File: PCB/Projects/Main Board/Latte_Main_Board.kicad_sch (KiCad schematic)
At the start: 115 parts, among them J1 SM02B-SURS-TF_LF__SN_, J2 SM02B-SURS-TF_LF__SN_, J3 Molex 505110-0892, J4 Molex 505110-0592, J5 Molex 505110-0892, J6 Molex 505110-0592, J8 Conn_01x04_Pin, J9 Molex 505110-1792, Q1 MMBT2222A, Q2 MMBT2222A, SW1 SW_Push, SW2 SW_Push, SW3 SW_Push, SW4 SW_Push, SW5 SW_Push, SW6 SW_Push, SW7 SW_Push, SW8 SW_Push, U1 HAL4395, U10 HAL4395, U11 HAL4395, U2 RP2350_80QFN, U3 HAL4395, U4 ST_LSM6, U5 ST_LSM6, U6 HAL4395, U7 HAL4395, U8 HAL4395, U9 HAL4395, Y1 ABM8-272-T3

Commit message: Routing updates
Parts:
- added R25, R28, R29, R31: 100R, Resistor_SMD:R_0201_0603Metric, symbol Device:R
- C39, C40: footprint RP2350_80QFN_minimal:C_0402_1005Metric_small_pads -> Capacitor_SMD:C_0402_1005Metric
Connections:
- net +3V3: now also C17.1, C18.1, C3.1, C4.1, C5.1, C6.1, C7.1, C8.1, U1.1 (VCC), U10.1 (VCC), U11.1 (VCC), U3.1 (VCC), U6.1 (VCC), U7.1 (VCC), U8.1 (VCC), U9.1 (VCC)
- net ABXY_EN: now also R31.2
- net DPAD_EN: now also R25.2
- net LRA_R: now also U2.26 (GPIO25); no longer U2.25 (GPIO24)
- net STICK_L_X_OUT: now also U2.57 (GPIO46_ADC6); no longer U2.56 (GPIO45_ADC5)
- net STICK_L_Y_OUT: now also U2.58 (GPIO47_ADC7); no longer U2.55 (GPIO44_ADC4)
- net STICK_R_X_OUT: now also U2.56 (GPIO45_ADC5); no longer U2.58 (GPIO47_ADC7)
- net STICK_R_Y_OUT: now also U2.55 (GPIO44_ADC4); no longer U2.57 (GPIO46_ADC6)
- net at R21.1: now also U2.37 (GPIO29); no longer U2.36 (GPIO28)
- net at R23.1: now also U2.48 (GPIO39); no longer U2.38 (GPIO30)
- net at U2.12 (GPIO13): now also R25.1
- net at U2.13 (GPIO14): now also R28.1
- net at R2.1: now also U2.27 (GPIO26); no longer U2.26 (GPIO25)
- net at U2.28 (GPIO27): now also R31.1
- net at R24.1: now also U2.36 (GPIO28); no longer U2.37 (GPIO29)
- net TRIGGER_EN renamed TRIGGER_EN_L
- net TRIGGER_EN_L: now also R28.2; no longer J4.2 (Pin_2)
- new net: R29.1, U2.25 (GPIO24)
- new net TRIGGER_EN_R: J4.2 (Pin_2), R29.2
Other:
- note added: "PWM4 B"
- note removed: "PWM4 A"
- moved on the sheet: R2, R21, R23, R24

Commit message: Routing Updates
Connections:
- net LRA_R+: now also J1.2; no longer J1.1
- net LRA_R-: now also J1.1; no longer J1.2
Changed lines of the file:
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@@
 	(global_label "LRA_R-"
 		(shape input)
+		(at 302.26 34.29 0)
+		(fields_autoplaced yes)
+		(effects
+			(font
+				(size 1.27 1.27)
+			)
+			(justify left)
+		)
+		(property "Intersheetrefs" "${INTERSHEET_REFS}"
+			(at 312.4419 34.29 0)
+			(effects
+				(font
+					(size 1.27 1.27)
+				)
+				(justify left)
+				(hide yes)
+			)
+		)
+	)
+	(global_label "ADC_2"
+		(shape input)
+		(at 139.7 -36.83 0)
+		(fields_autoplaced yes)
+		(effects
+			(font
+				(size 1.27 1.27)
+			)
+			(justify left)
+		)
+		(property "Intersheetrefs" "${INTERSHEET_REFS}"
+			(at 148.4909 -36.83 0)
+			(effects
+				(font
+					(size 1.27 1.27)
+				)
+				(justify left)
+				(hide yes)
+			)
+		)
+	)
+	(global_label "I2C1_SCL"
+		(shape input)
+		(at 204.47 130.81 0)
+		(fields_autoplaced yes)
+		(effects
+			(font
+				(size 1.27 1.27)
+			)
+			(justify left)
+		)
+		(property "Intersheetrefs" "${INTERSHEET_REFS}"
+			(at 216.2242 130.81 0)
+			(effects
+				(font
+					(size 1.27 1.27)
+				)
+				(justify left)
+				(hide yes)
+			)
+		)
+	)
+	(global_label "WL_CLK"
+		(shape input)
+		(at 148.59 139.7 0)
+		(fields_autoplaced yes)
+		(effects
+			(font
+				(size 1.27 1.27)
+			)
+			(justify left)
+		)
+		(property "Intersheetrefs" "${INTERSHEET_REFS}"
+			(at 157.9362 139.7 0)
+			(effects
+				(font
+					(size 1.27 1.27)
+				)
+				(justify left)
+				(hide yes)
+			)
+		)
+	)
+	(global_label "SPI1_RX"
+		(shape input)
+		(at 441.96 113.03 180)
+		(fields_autoplaced yes)
+		(effects
+			(font
+				(size 1.27 1.27)
+			)
+			(justify right)
+		)
+		(property "Intersheetrefs" "${INTERSHEET_REFS}"
+			(at 431.2339 113.03 0)
+			(effects
+				(font
+					(size 1.27 1.27)
+				)
+				(justify right)
+				(hide yes)
+			)
+		)
+	)
+	(global_label "STICK_R_RGB_OUT"
+		(shape input)
+		(at 290.83 227.33 180)
+		(fields_autoplaced yes)
+		(effects
+			(font
+				(size 1.27 1.27)
+			)
+			(justify right)
+		)
+		(property "Intersheetrefs" "${INTERSHEET_REFS}"
+			(at 270.9115 227.33 0)
+			(effects
+				(font
+					(size 1.27 1.27)
+				)
+				(justify right)
+				(hide yes)
+			)
+		)
+	)
+	(global_label "N_DATA_3.3"
+		(shape input)
+		(at 204.47 128.27 0)
+		(fields_autoplaced yes)
+		(effects
+			(font
+				(size 1.27 1.27)
+			)
+			(justify left)
+		)
+		(property "Intersheetrefs" "${INTERSHEET_REFS}"
+			(at 217.4985 128.3494 0)
+			(effects
+				(font
+					(size 1.27 1.27)
+				)
+				(justify left)
+				(hide yes)
+			)
+		)
+	)
+	(global_label "SWD"
+		(shape input)
+		(at 73.66 189.23 180)
+		(fields_autoplaced yes)
+		(effects
+			(font
+				(size 1.27 1.27)
+			)
+			(justify right)
+		)
+		(property "Intersheetrefs" "${INTERSHEET_REFS}"
+			(at 66.7439 189.23 0)
+			(effects
+				(font
+					(size 1.27 1.27)
+				)
+				(justify right)
+				(hide yes)
+			)
+		)
+	)
+	(global_label "I2C1_SDA"
+		(shape input)
+		(at 443.23 90.17 270)
+		(fields_autoplaced yes)
+		(effects
+			(font
+				(size 1.27 1.27)
+			)
+			(justify right)
+		)
+		(property "Intersheetrefs" "${INTERSHEET_REFS}"
+			(at 443.23 101.3305 90)
+			(effects
+				(font
+					(size 1.27 1.27)
+				)
+				(justify right)
+				(hide yes)
+			)
+		)
+	)
+	(global_label "ADC_0"
+		(shape input)
+		(at 139.7 -72.39 0)
+		(fields_autoplaced yes)
+		(effects
+			(font
+				(size 1.27 1.27)
+			)
+			(justify left)
+		)
+		(property "Intersheetrefs" "${INTERSHEET_REFS}"
+			(at 148.4909 -72.39 0)
+			(effects
+				(font
+					(size 1.27 1.27)
+				)
+				(justify left)
+				(hide yes)
+			)
+		)
+	)
+	(global_label "LRA_L"
+		(shape input)
+		(at 157.48 152.4 0)
+		(fields_autoplaced yes)
+		(effects
+			(font
+				(size 1.27 1.27)
+			)
+			(justify left)
+		)
+		(property "Intersheetrefs" "${INTERSHEET_REFS}"
+			(at 165.8476 152.4 0)
+			(effects
+				(font
+					(size 1.27 1.27)
+				)
+				(justify left)
+				(hide yes)
+			)
+		)
+	)
+	(global_label "LRA_R+"
+		(shape input)
 		(at 302.26 31.75 0)
 		(fields_autoplaced yes)
@@
 			(effects
 				(font
-					(size 1.27 1.27)
-				)
-				(justify left)
-				(hide yes)
-			)
-		)
-	)
-	(global_label "ADC_2"
-		(shape input)
-		(at 139.7 -36.83 0)
-		(fields_autoplaced yes)
-		(effects
-			(font
-				(size 1.27 1.27)
-			)
-			(justify left)
-		)
-		(property "Intersheetrefs" "${INTERSHEET_REFS}"
-			(at 148.4909 -36.83 0)
-			(effects
-				(font
-					(size 1.27 1.27)
-				)
-				(justify left)
-				(hide yes)
-			)
-		)
-	)
-	(global_label "I2C1_SCL"
-		(shape input)
-		(at 204.47 130.81 0)
-		(fields_autoplaced yes)
-		(effects
-			(font
-				(size 1.27 1.27)
-			)
-			(justify left)
-		)
-		(property "Intersheetrefs" "${INTERSHEET_REFS}"
-			(at 216.2242 130.81 0)
-			(effects
-				(font
-					(size 1.27 1.27)
-				)
-				(justify left)
-				(hide yes)
-			)
-		)
-	)
-	(global_label "WL_CLK"
-		(shape input)
-		(at 148.59 139.7 0)
-		(fields_autoplaced yes)
-		(effects
-			(font
-				(size 1.27 1.27)
-			)
-			(justify left)
-		)
-		(property "Intersheetrefs" "${INTERSHEET_REFS}"
-			(at 157.9362 139.7 0)
-			(effects
-				(font
-					(size 1.27 1.27)
-				)
-				(justify left)
-				(hide yes)
-			)
-		)
-	)
-	(global_label "SPI1_RX"
-		(shape input)
-		(at 441.96 113.03 180)
-		(fields_autoplaced yes)
-		(effects
-			(font
-				(size 1.27 1.27)
-			)
-			(justify right)
-		)
-		(property "Intersheetrefs" "${INTERSHEET_REFS}"
-			(at 431.2339 113.03 0)
-			(effects
-				(font
-					(size 1.27 1.27)
-				)
-				(justify right)
-				(hide yes)
-			)
-		)
-	)
-	(global_label "STICK_R_RGB_OUT"
-		(shape input)
-		(at 290.83 227.33 180)
-		(fields_autoplaced yes)
-		(effects
-			(font
-				(size 1.27 1.27)
-			)
-			(justify right)
-		)
-		(property "Intersheetrefs" "${INTERSHEET_REFS}"
-			(at 270.9115 227.33 0)
-			(effects
-				(font
-					(size 1.27 1.27)
-				)
-				(justify right)
-				(hide yes)
-			)
-		)
-	)
-	(global_label "N_DATA_3.3"
-		(shape input)
-		(at 204.47 128.27 0)
-		(fields_autoplaced yes)
-		(effects
-			(font
-				(size 1.27 1.27)
-			)
-			(justify left)
-		)
-		(property "Intersheetrefs" "${INTERSHEET_REFS}"
-			(at 217.4985 128.3494 0)
-			(effects
-				(font
-					(size 1.27 1.27)
-				)
-				(justify left)
-				(hide yes)
-			)
-		)
-	)
-	(global_label "SWD"
-		(shape input)
-		(at 73.66 189.23 180)
-		(fields_autoplaced yes)
-		(effects
-			(font
-				(size 1.27 1.27)
-			)
-			(justify right)
-		)
-		(property "Intersheetrefs" "${INTERSHEET_REFS}"
-			(at 66.7439 189.23 0)
-			(effects
-				(font
-					(size 1.27 1.27)
-				)
-				(justify right)
-				(hide yes)
-			)
-		)
-	)
-	(global_label "I2C1_SDA"
-		(shape input)
-		(at 443.23 90.17 270)
-		(fields_autoplaced yes)
-		(effects
-			(font
-				(size 1.27 1.27)
-			)
-			(justify right)
-		)
-		(property "Intersheetrefs" "${INTERSHEET_REFS}"
-			(at 443.23 101.3305 90)
-			(effects
-				(font
-					(size 1.27 1.27)
-				)
-				(justify right)
-				(hide yes)
-			)
-		)
-	)
-	(global_label "ADC_0"
-		(shape input)
-		(at 139.7 -72.39 0)
-		(fields_autoplaced yes)
-		(effects
-			(font
-				(size 1.27 1.27)
-			)
-			(justify left)
-		)
-		(property "Intersheetrefs" "${INTERSHEET_REFS}"
-			(at 148.4909 -72.39 0)
-			(effects
-				(font
-					(size 1.27 1.27)
-				)
-				(justify left)
-				(hide yes)
-			)
-		)
-	)
-	(global_label "LRA_L"
-		(shape input)
-		(at 157.48 152.4 0)
-		(fields_autoplaced yes)
-		(effects
-			(font
-				(size 1.27 1.27)
-			)
-			(justify left)
-		)
-		(property "Intersheetrefs" "${INTERSHEET_REFS}"
-			(at 165.8476 152.4 0)
-			(effects
-				(font
-					(size 1.27 1.27)
-				)
-				(justify left)
-				(hide yes)
-			)
-		)
-	)
-	(global_label "LRA_R+"
-		(shape input)
-		(at 302.26 34.29 0)
-		(fields_autoplaced yes)
-		(effects
-			(font
-				(size 1.27 1.27)
-			)
-			(justify left)
-		)
-		(property "Intersheetrefs" "${INTERSHEET_REFS}"
-			(at 312.4419 34.29 0)
-			(effects
-				(font

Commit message: Routing updates
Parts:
- U4, U5: LCSC C784817 -> C126672; MPN LSM6DSRTR -> LSM6DSLTR
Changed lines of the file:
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@@
 			)
 		)
-		(property "LCSC" "C784817"
+		(property "LCSC" "C126672"
 			(at 453.39 156.21 0)
 			(effects
@@
 			)
 		)
-		(property "MPN" "LSM6DSRTR"
+		(property "MPN" "LSM6DSLTR"
 			(at 453.39 156.21 0)
 			(effects
@@
 			)
 		)
-		(property "LCSC" "C784817"
+		(property "LCSC" "C126672"
 			(at 453.39 116.84 0)
 			(effects
@@
 			)
 		)
-		(property "MPN" "LSM6DSRTR"
+		(property "MPN" "LSM6DSLTR"
 			(at 453.39 116.84 0)
 			(effects

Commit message: Routing updates
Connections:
- net GND: now also SW3.1, SW4.1, SW5.1, SW6.1, SW7.1, SW8.1, U2.81 (GND)
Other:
- moved on the sheet: SW5, SW6, SW7, SW8

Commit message: Routing updates
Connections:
- net GND: now also SW2.1; no longer R15.2
- net at R15.1: now also U2.35 (RUN); no longer SW2.1
- net at SW2.2: now also R15.2; no longer U2.35 (RUN)
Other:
- moved on the sheet: C10, C11, C12, C13, C14, C17, C18, C19, C23, C24, C25, C26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

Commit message: Prod 1
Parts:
- C17, C18, C19, C29, C3, C30, C31, C32, C33, C34, C35, C36, C37, C38, C4, C5, C6, C7, C8: LCSC (none) -> C76934; MPN (none) -> GRM033R61A104KE15D; Manufacturer (none) -> muRata
- C23, C39, C40, C41: LCSC (none) -> C541464; MPN (none) -> CC0402JRX7R7BB104; Manufacturer (none) -> YAGEO
- L1: LCSC (none) -> C42411119; MPN (none) -> AOTA-B201610S3R3-101-T; Manufacturer (none) -> Abraco LLC
- R11: LCSC (none) -> C295794; MPN (none) -> RC0201FR-0733RL; Manufacturer (none) -> YAGEO
- R15: LCSC (none) -> C138165; MPN (none) -> RC0201FR-071KL; Manufacturer (none) -> YAGEO
- SW1, SW2, SW3, SW4, SW5, SW6, SW7, SW8: LCSC (none) -> C221725; Manufacturer (none) -> C&K
- U1, U10, U11, U3, U6, U7, U8, U9: LCSC (none) -> C49165022; MPN (none) -> HAL4395SO5; Manufacturer (none) -> Hallwee
- U2: LCSC (none) -> C39843328; MPN (none) -> RP2354B; Manufacturer (none) -> Raspberry Pi

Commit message: 3D Files Initial STLs
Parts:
- C23, C39, C40, C41: LCSC C541464 -> C368809; MPN CC0402JRX7R7BB104 -> CL05A475KP5NRNC; Manufacturer YAGEO -> Samsung Electro-Mechanics
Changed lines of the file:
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@@
 			)
 		)
-		(property "Description" "16V 100nF X7R ±5% 0402 Ceramic Capacitors RoHS"
-			(at 62.23 99.06 0)
+		(property "Description" "10V 4.7uF X5R ±10% 0402 Ceramic Capacitors RoHS"
+			(at 61.468 106.172 0)
 			(effects
 				(font
 					(size 1.27 1.27)
 				)
+				(hide yes)
 			)
 		)
@@
 			)
 		)
-		(property "LCSC" "C541464"
+		(property "LCSC" "C368809"
 			(at 62.23 99.06 0)
 			(effects
@@
 			)
 		)
-		(property "MPN" "CC0402JRX7R7BB104"
+		(property "MPN" "CL05A475KP5NRNC"
 			(at 62.23 99.06 0)
 			(effects
@@
 			)
 		)
-		(property "Manufacturer" "YAGEO"
+		(property "Manufacturer" "Samsung Electro-Mechanics"
 			(at 62.23 99.06 0)
 			(effects
@@
 		(on_board yes)
 		(dnp no)
-		(fields_autoplaced yes)
 		(property "Reference" "C40"
 			(at 30.48 139.7 0)
@@
 			)
 		)
-		(property "Description" "16V 100nF X7R ±5% 0402 Ceramic Capacitors RoHS"
-			(at 26.67 140.97 0)
+		(property "Description" "10V 4.7uF X5R ±10% 0402 Ceramic Capacitors RoHS"
+			(at 25.908 146.304 0)
 			(effects
 				(font
 					(size 1.27 1.27)
 				)
+				(hide yes)
 			)
 		)
@@
 			)
 		)
-		(property "LCSC" "C541464"
+		(property "LCSC" "C368809"
 			(at 26.67 140.97 0)
 			(effects
@@
 			)
 		)
-		(property "MPN" "CC0402JRX7R7BB104"
+		(property "MPN" "CL05A475KP5NRNC"
 			(at 26.67 140.97 0)
 			(effects
@@
 			)
 		)
-		(property "Manufacturer" "YAGEO"
+		(property "Manufacturer" "Samsung Electro-Mechanics"
 			(at 26.67 140.97 0)
 			(effects
@@
 					(size 1.27 1.27)
 				)
+				(hide yes)
 			)
 		)
@@
 					(size 1.27 1.27)
 				)
+				(hide yes)
 			)
 		)
@@
 					(size 1.27 1.27)
 				)
+				(hide yes)
 			)
 		)
@@
 					(size 1.27 1.27)
 				)
+				(hide yes)
 			)
 		)
@@
 					(size 1.27 1.27)
 				)
+				(hide yes)
 			)
 		)
@@
 					(size 1.27 1.27)
 				)
+				(hide yes)
 			)
 		)
@@
 		(on_board yes)
 		(dnp no)
-		(fields_autoplaced yes)
 		(property "Reference" "L1"
 			(at 43.18 139.7 0)
@@
 		)
 		(property "Description" "0806 POLARIZED Fixed Inductors RoHS"
-			(at 41.91 140.97 0)
+			(at 40.894 145.034 0)
 			(effects
 				(font
 					(size 1.27 1.27)
 				)
+				(hide yes)
 			)
 		)
@@
 					(size 1.27 1.27)
 				)
+				(hide yes)
 			)
 		)
@@
 					(size 1.27 1.27)
 				)
+				(hide yes)
 			)
 		)
@@
 					(size 1.27 1.27)
 				)
+				(hide yes)
 			)
 		)
@@
 					(size 1.27 1.27)
 				)
+				(hide yes)
 			)
 		)
@@
 					(size 1.27 1.27)
 				)
+				(hide yes)
 			)
 		)
@@
 					(size 1.27 1.27)
 				)
+				(hide yes)
 			)
 		)
@@
 					(size 1.27 1.27)
 				)
+				(hide yes)
 			)
 		)
@@
 					(size 1.27 1.27)
 				)
+				(hide yes)
 			)
 		)
@@
 					(size 1.27 1.27)
 				)
+				(hide yes)
 			)
 		)
@@
 					(size 1.27 1.27)
 				)
+				(hide yes)
 			)
 		)
@@
 			)
 		)
-		(property "Description" "16V 100nF X7R ±5% 0402 Ceramic Capacitors RoHS"
+		(property "Description" "10V 4.7uF X5R ±10% 0402 Ceramic Capacitors RoHS"
 			(at 60.96 128.27 0)
 			(effects
@@
 					(size 1.27 1.27)
 				)
+				(hide yes)
 			)
 		)
@@
 			)
 		)
-		(property "LCSC" "C541464"
+		(property "LCSC" "C368809"
 			(at 60.96 128.27 0)
 			(effects
@@
 			)
 		)
-		(property "MPN" "CC0402JRX7R7BB104"
+		(property "MPN" "CL05A475KP5NRNC"
 			(at 60.96 128.27 0)
 			(effects
@@
 			)
 		)
-		(property "Manufacturer" "YAGEO"
+		(property "Manufacturer" "Samsung Electro-Mechanics"
 			(at 60.96 128.27 0)
 			(effects
@@
 					(size 1.27 1.27)
 				)
+				(hide yes)
 			)
 		)
@@
 					(size 1.27 1.27)
 				)
+				(hide yes)
 			)
 		)
@@
 					(size 1.27 1.27)
 				)
+				(hide yes)
 			)
 		)
@@
 			)
 		)
-		(property "Description" "16V 100nF X7R ±5% 0402 Ceramic Capacitors RoHS"
+		(property "Description" "10V 4.7uF X5R ±10% 0402 Ceramic Capacitors RoHS"
 			(at 15.24 140.97 0)
 			(effects
@@
 					(size 1.27 1.27)
 				)
+				(hide yes)
 			)
 		)
@@
 			)
 		)
-		(property "LCSC" "C541464"
+		(property "LCSC" "C368809"
 			(at 15.24 140.97 0)
 			(effects
@@
 			)
 		)
-		(property "MPN" "CC0402JRX7R7BB104"
+		(property "MPN" "CL05A475KP5NRNC"
 			(at 15.24 140.97 0)
 			(effects
@@
 			)
 		)
-		(property "Manufacturer" "YAGEO"
+		(property "Manufacturer" "Samsung Electro-Mechanics"
 			(at 15.24 140.97 0)
 			(effects
@@
 					(size 1.27 1.27)
 				)
+				(hide yes)
 			)
 		)

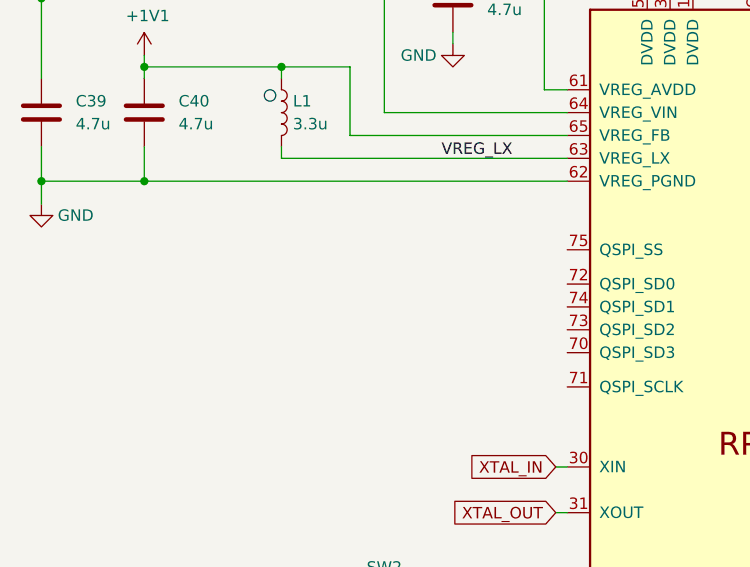
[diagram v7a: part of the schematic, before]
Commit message: PCB Update
- Missing BOOT switch added
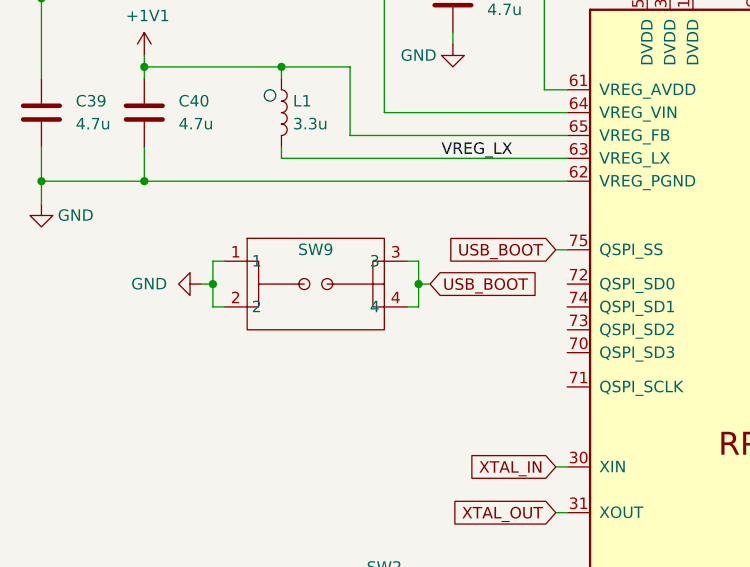
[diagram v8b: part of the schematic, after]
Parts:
- added SW9: 1TS026A-1000-0550, hhl:1TS026A-1000-0550, symbol hhl:1TS026A-1000-0550
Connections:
- net GND: now also SW9.1, SW9.2
- net USB_BOOT: now reaches U2.75 (QSPI_SS)
- net USB_BOOT: now also SW9.3, SW9.4
